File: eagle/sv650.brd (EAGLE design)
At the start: 54.2 x 52.1 mm, 22 parts, among them IC2 LM7805

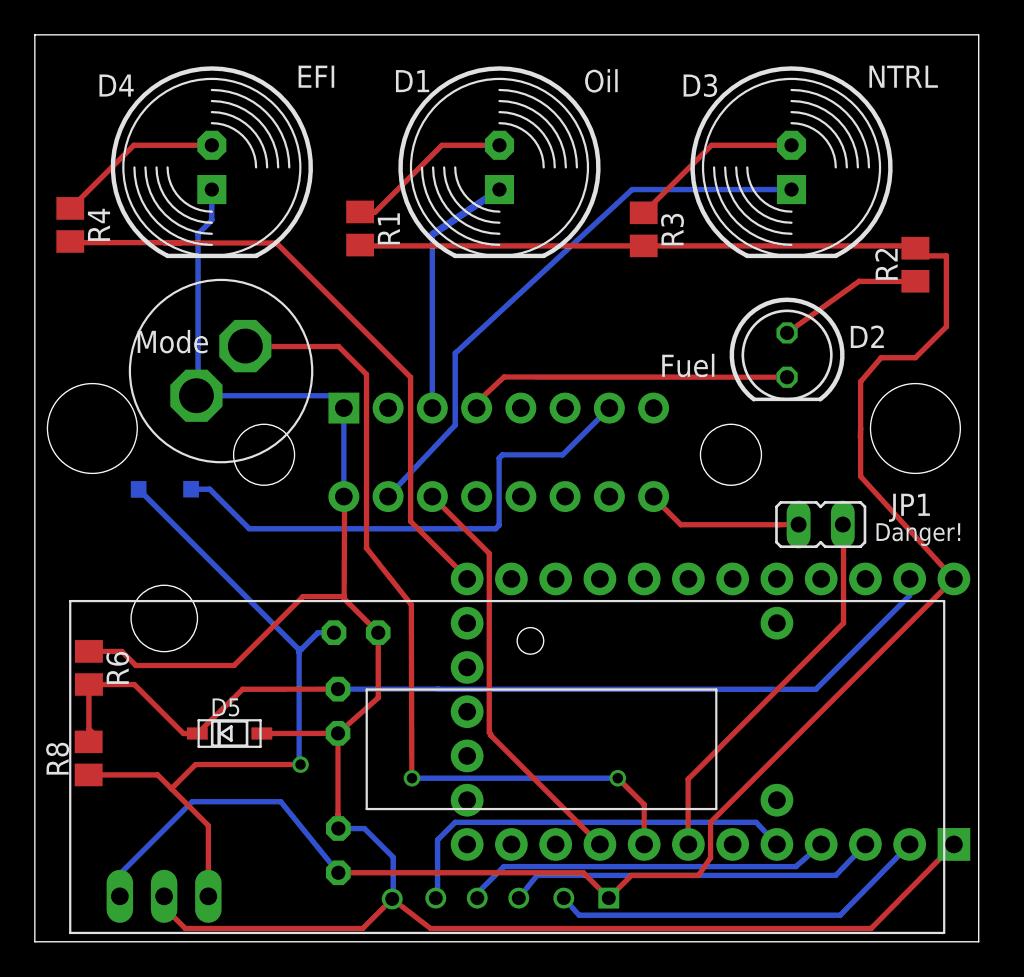
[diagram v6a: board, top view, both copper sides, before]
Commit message: update board to v4.3 - switch to LM2674-5.0 - Fix 20V schottky diode
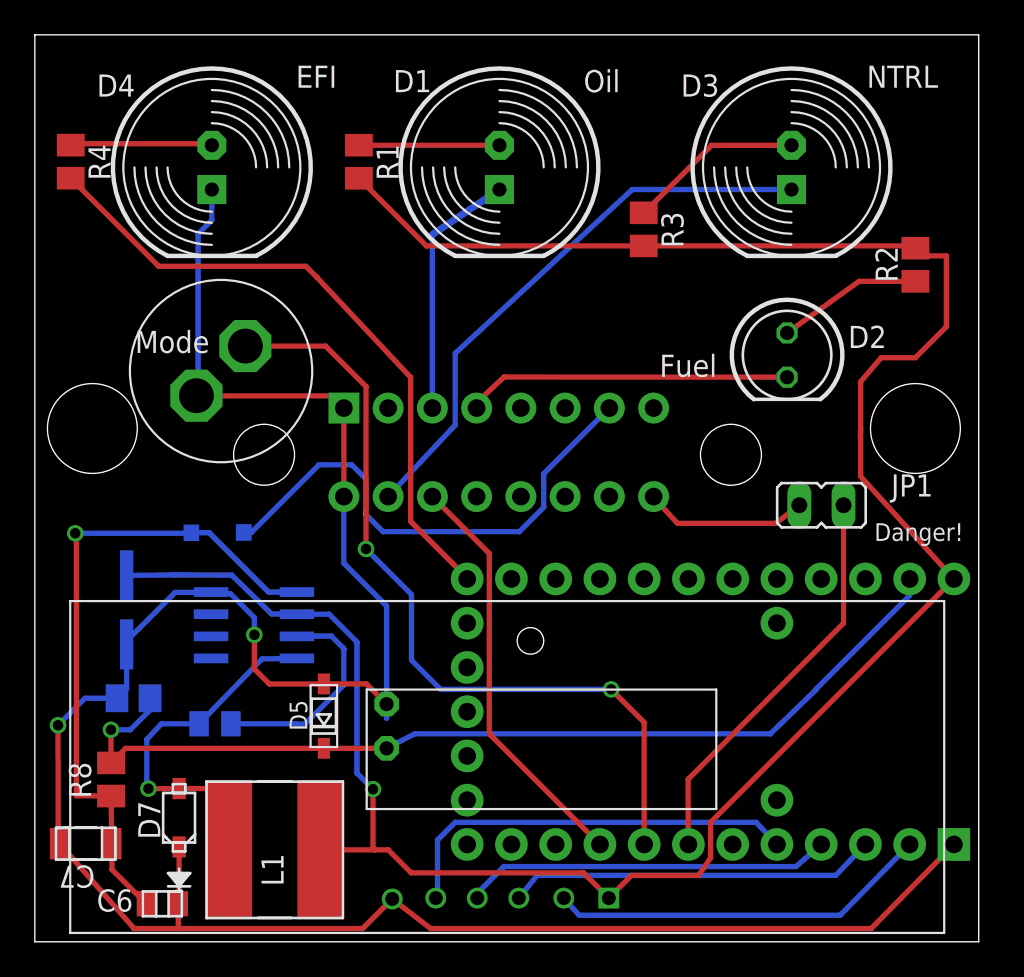
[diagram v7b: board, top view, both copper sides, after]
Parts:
- removed C1: .33uF, adafruit:C025-024X044
- removed C2: .1uF, adafruit:C025-024X044
- removed IC2: LM7805, synfinatic:TO220-SINK
- added C4: .01uF, TI-LM2674:0805
- added C5: 10uF, TI-LM2674:SM_RADIAL_C
- added C6: .1uF, TI-LM2674:0805
- added C7: 1uF, TI-LM2674:1206
- added D7: 40V/500mA, TI-LM2674:SOD-123
- added L1: 220uH/960mOhm, TI-LM2674:SDR0805
- added U$2: LM2674MX-5.0/NOPB, TI-LM2674:M08A
- moved D5 5.50 mm to (16.6, 13.0), turned to 90 degrees
- moved R1 3.83 mm to (18.6, 44.8)
- moved R4 3.63 mm to (2.06, 44.8)
- moved R6 3.10 mm to (5.67, 14.0), flipped to the bottom, turned to 180 degrees
- moved C3 2.92 mm to (20.2, 12.4), turned to 90 degrees
- moved D6 1.95 mm to (8.35, 24.0), turned to 180 degrees
- moved R8 1.77 mm to (4.38, 9.32)
- moved JP1 1.11 mm to (45.1, 25.1)
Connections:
- new net N$13: C4.2, U$2.1
- new net N$14: C4.1, D7.1, L1.2, U$2.8
- net +12V: now also C6.1, C7.1, D6.A, U$2.7; no longer C1.1, D6.C, IC2.IN
- net 5V: now also C5.1, L1.1, U$2.4; no longer C2.1, IC2.OUT
- net GND: now also C5.2, C6.2, C7.2, D7.2, U$2.6; no longer C1.2, C2.2, IC2.GND
- net N$12: now also D6.C; no longer D6.A
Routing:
- net N$14: track 0.00 -> 21.2 mm, vias 0 -> 1
- net GND: track 124.0 -> 137.0 mm, vias 0 -> 2
- net 5V: track 121.9 -> 134.8 mm, vias 0 -> 1
- net N$13: track 0.00 -> 12.5 mm
- net +12V: track 42.3 -> 38.2 mm
- net N$8: track 9.73 -> 8.08 mm
- net R2: track 9.63 -> 8.17 mm
- net MODE: track 48.0 -> 46.5 mm
- net N$9: track 36.6 -> 37.3 mm
- net N$12: track 30.1 -> 29.5 mm
- net BATTMON: vias 0 -> 1
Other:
- board text added: "20140321"
- board text added: "http://synfin.net/sv650ecu SV650 ECU Decoder v4.3"
- board text removed: "20140310"
- board text removed: "http://synfin.net/sv650ecu SV650 ECU Decoder v4.2"

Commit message: Fuel level LED is now controlled by Teensy     Use LT082CP to measure fuel sensor     add 5W 82ohm resistor to fuel line     Remove Fuel2 jumper/support
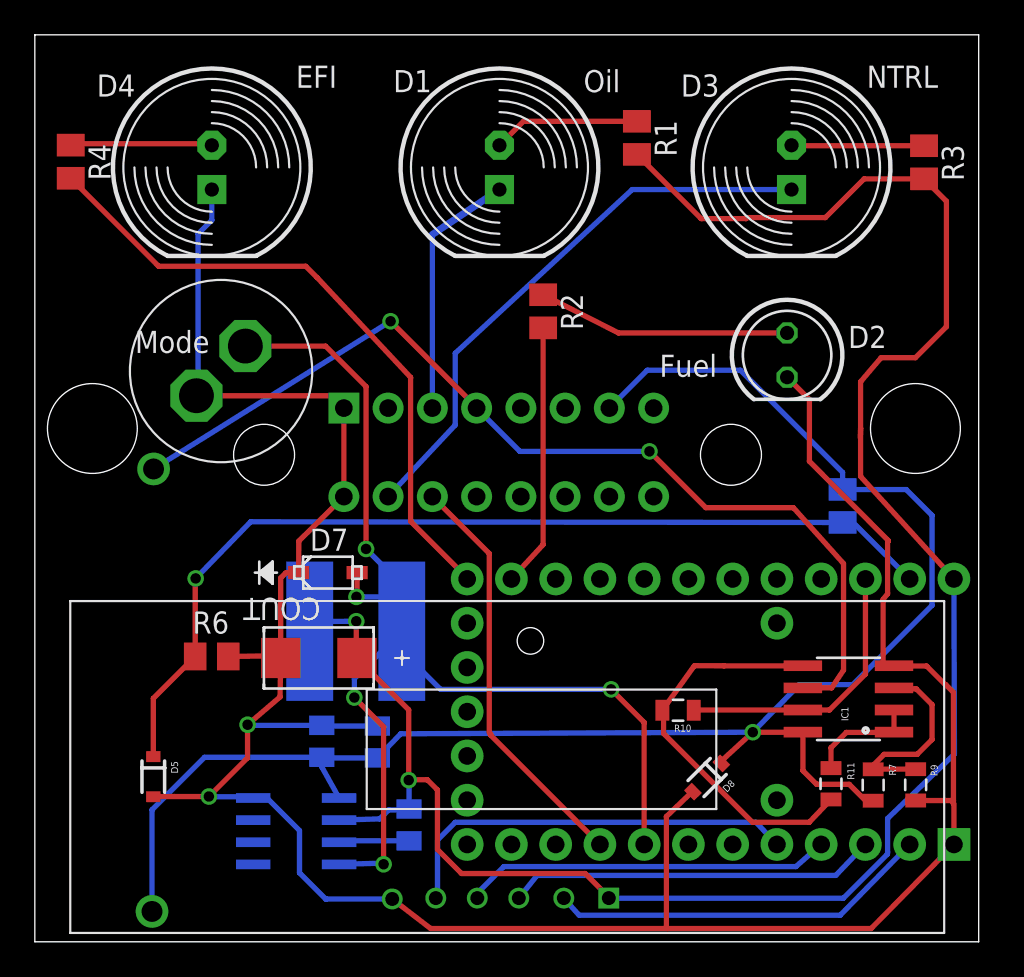
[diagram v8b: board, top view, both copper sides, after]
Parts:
- removed C3: .1uF, adafruit:C025-024X044
- removed C4: .01uF, TI-LM2674:0805
- removed C5: 10uF, TI-LM2674:SM_RADIAL_C
- removed C6: .1uF, TI-LM2674:0805
- removed C7: 1uF, TI-LM2674:1206
- removed D6: 20V schottky, synfinatic:SOD-123
- removed JP1: (no value), jumper:JP1
- added CB: .01uF, TI-LM2674:0805
- added CIN: 1uF, TI-LM2674:0805
- added CINX: .1uF, TI-LM2674:0805
- added COUT: 22uF, TI-LM2674:6032-28
- added D8: 16V Zener, SparkFun-DiscreteSemi:SOD-323
- added IC1: TL082CP, SparkFun-AnalogIC:SO08
- added R10: 10k, synfinatic:0805
- added R11: 100, synfinatic:0805
- added R5: 82, synfinatic:AXIAL-0.9
- added R7: 3.3k, synfinatic:0805
- added R9: 5.6k, synfinatic:0805
- D5: value 4.7V zener -> 5.1V Zener; device adafruit:SOD-123 -> SparkFun-DiscreteSemi:SOD-323
- D7: value 40V/500mA -> 510mV
- L1: value 220uH/960mOhm -> 220uH
- R6: value 10k -> 13.3k
- moved R8 44.8 mm to (46.4, 25.0), flipped to the bottom, turned to 90 degrees
- moved R2 21.5 mm to (29.2, 36.2), turned to 270 degrees
- moved R3 16.5 mm to (51.0, 44.7)
- moved D7 16.5 mm to (16.8, 21.2), turned to 0 degrees
- moved R1 16.0 mm to (34.6, 46.1)
- moved L1 13.4 mm to (18.4, 17.8), flipped to the bottom
- moved U$2 12.1 mm to (15.0, 6.35)
- moved D5 10.4 mm to (6.80, 9.48), turned to 270 degrees
- moved R6 5.09 mm to (10.2, 16.4), flipped to the top
- renumbered _1 to $U3
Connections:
- removed net LOWFUEL2: JP1.2, U$3.P$16
- removed net N$12: D6.C, U$3.P$7
- new net FUEL_ADC: $U3.F1, IC1.7, R10.1
- new net N$15: D7.1, L1.2, U$2.8
- new net N$16: $U3.D7, R2.2
- new net N$17: IC1.3, R7.1, R9.2
- new net N$20: IC1.5, R10.2, R11.2
- net +12V: now also CIN.1, CINX.1, D8.C, IC1.8, R5.P$2, R7.2, U$3.P$7; no longer C6.1, C7.1, D6.A
- net 5V: now also CB.1, COUT.1; no longer C5.1, R2.2
- net BATTMON: no longer C3.1
- net FUEL: now also IC1.6, R5.P$1; no longer D2.K
- net FUEL2: now also U$3.P$16; no longer $U3.D0, JP1.1
- net GND: now also CIN.2, CINX.2, COUT.2, D2.K, D8.A, IC1.4, R9.1; no longer C3.2, C5.2, C6.2, C7.2
- net N$13: now also CB.2; no longer C4.2
- net N$14: now also IC1.1, IC1.2, R11.1; no longer C4.1, D7.1, L1.2, U$2.8
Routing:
- net +12V: track 38.2 -> 99.7 mm
- net FUEL: track 18.7 -> 56.9 mm, vias 0 -> 2
- net N$12: track 29.5 -> 0.00 mm
- net N$15: track 0.00 -> 23.9 mm, vias 0 -> 3
- net N$20: track 0.00 -> 23.0 mm
- net FUEL2: track 22.0 -> 0.00 mm
- net GND: track 137.0 -> 153.5 mm
- net FUEL_ADC: track 0.00 -> 16.2 mm
- net 5V: track 134.8 -> 118.8 mm, vias 1 -> 3
- net N$16: track 0.00 -> 15.1 mm
- net N$14: track 21.2 -> 6.43 mm, vias 1 -> 0
- net N$17: track 0.00 -> 12.6 mm
- net LOWFUEL2: track 9.42 -> 0.00 mm
- net N$13: track 12.5 -> 4.02 mm
- net N$7: track 8.32 -> 14.5 mm
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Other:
- board text removed: "Danger!"
